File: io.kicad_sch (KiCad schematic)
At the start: 15 parts, among them J14 D IN1, J15 D IN2, J16 D IN3

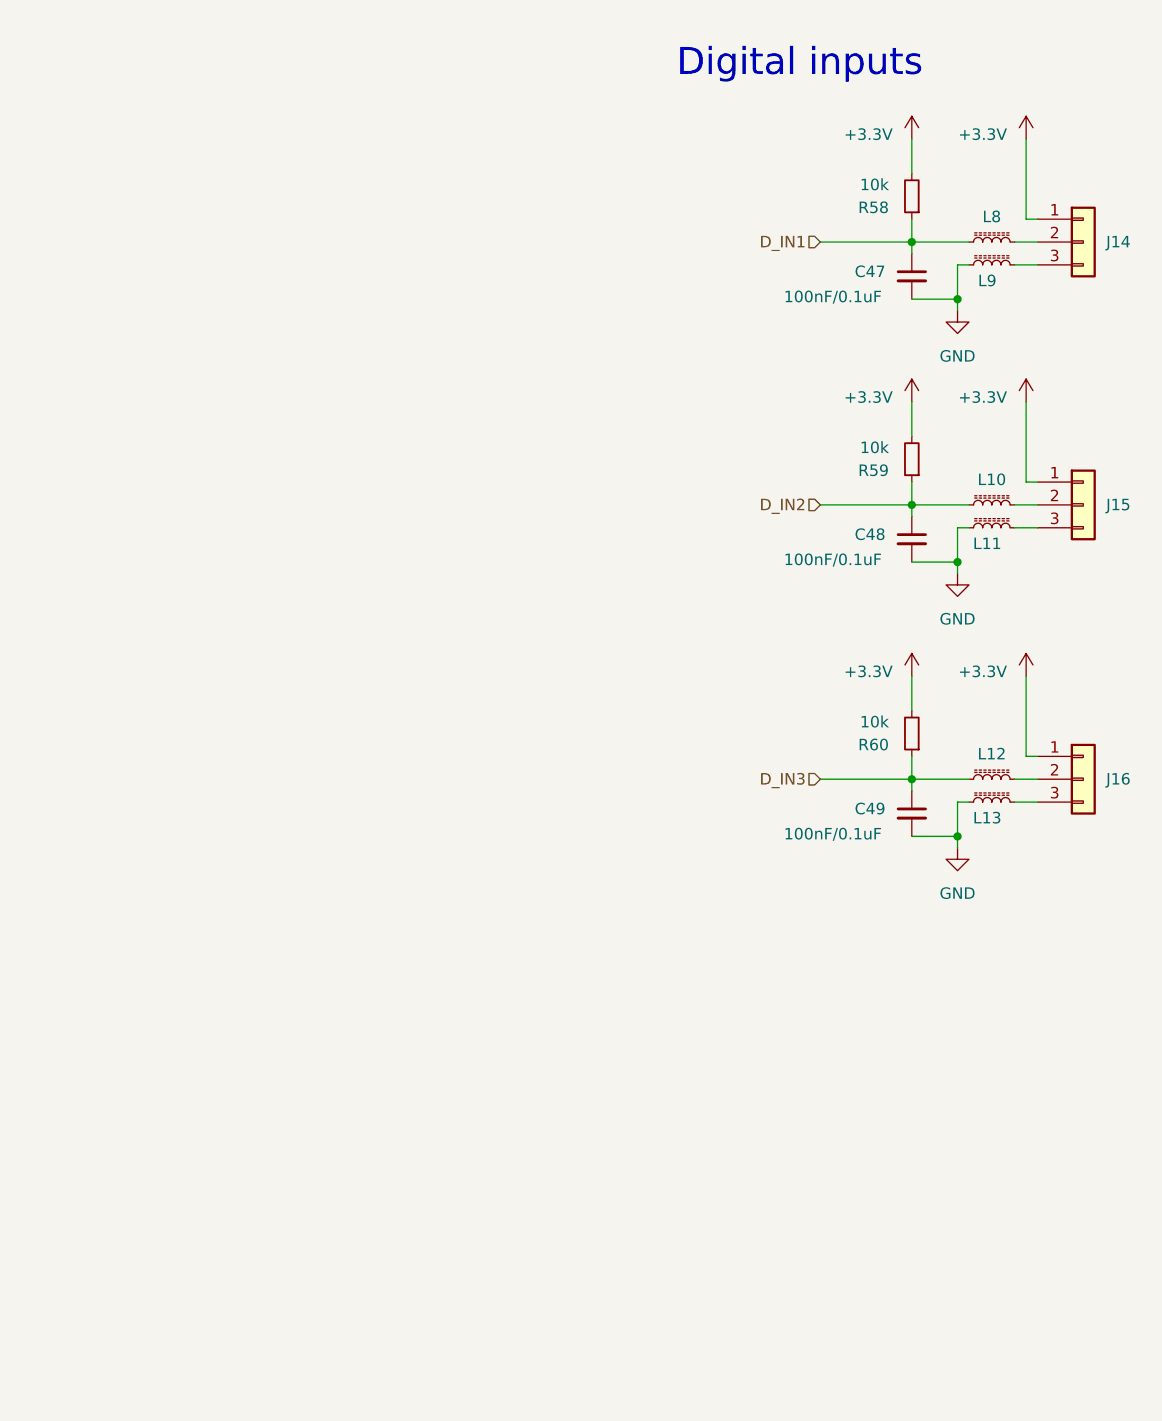
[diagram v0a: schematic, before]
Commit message: Add 1-Wire
Closes #29
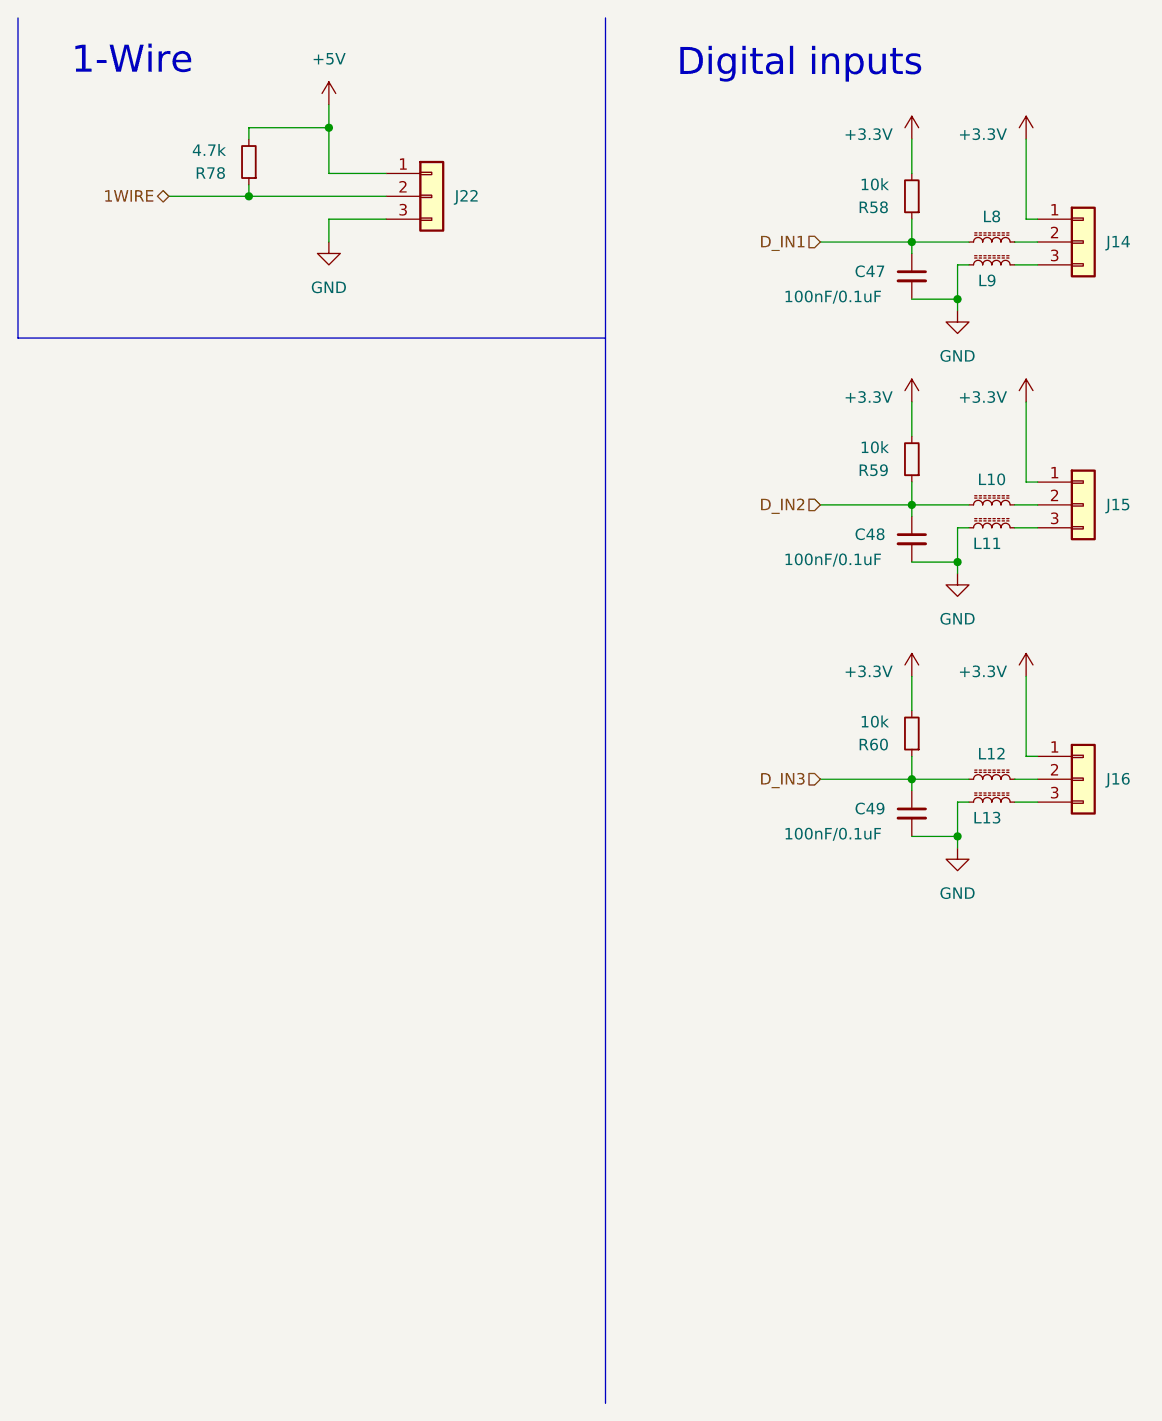
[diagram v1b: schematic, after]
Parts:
- added J22: 1-Wire, Connector_PinHeader_2.54mm:PinHeader_1x03_P2.54mm_Vertical, symbol Connector_Generic:Conn_01x03
- added R78: 4.7k, Resistor_SMD:R_0603_1608Metric, symbol Device:R_Small
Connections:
- net GND: now also J22.3 (Pin_3)
- new net +5V: J22.1 (Pin_1), R78.2
- new net 1WIRE: J22.2 (Pin_2), R78.1
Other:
- note added: "1-Wire"

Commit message: Update manufacturing positions and rotations of parts
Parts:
- J14, J15, J16: JLCPCB Position Offset (none) -> 0,2; JLCPCB Rotation Offset (none) -> 180
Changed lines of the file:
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@@
+			)
+		)
+		(property "JLCPCB Rotation Offset" "180"
+			(at 261.62 66.04 0)
+			(effects
+				(font
+					(size 1.27 1.27)
+				)
+				(hide yes)
+			)
+		)
+		(property "JLCPCB Position Offset" "0,2"
+			(at 261.62 66.04 0)
+			(effects
+				(font
+					(size 1.27 1.27)
+				)
+				(hide yes)
 			)
 		)
@@
 			)
 		)
+		(property "JLCPCB Rotation Offset" "180"
+			(at 261.62 36.83 0)
+			(effects
+				(font
+					(size 1.27 1.27)
+				)
+				(hide yes)
+			)
+		)
+		(property "JLCPCB Position Offset" "0,2"
+			(at 261.62 36.83 0)
+			(effects
+				(font
+					(size 1.27 1.27)
+				)
+				(hide yes)
+			)
+		)
 		(pin "2"
 		)
@@
 			(at 261.62 96.52 0)
 			(effects
+				(font
+					(size 1.27 1.27)
+				)
+				(hide yes)
+			)
+		)
+		(property "JLCPCB Rotation Offset" "180"
+			(at 261.62 96.52 0)
+			(effects
+				(font
+					(size 1.27 1.27)
+				)
+				(hide yes)
+			)
+		)
+		(property "JLCPCB Position Offset" "0,2"
+			(at 261.62 96.52 0)
+			(effects

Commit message: Include THT components in manufacturing
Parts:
- J14, J15, J16: now in the parts list
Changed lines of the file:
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@@
 		(unit 1)
 		(exclude_from_sim no)
-		(in_bom no)
+		(in_bom yes)
 		(on_board yes)
 		(dnp no)
@@
 		(unit 1)
 		(exclude_from_sim no)
-		(in_bom no)
+		(in_bom yes)
 		(on_board yes)
 		(dnp no)
@@
 		(unit 1)
 		(exclude_from_sim no)
-		(in_bom no)
-		(on_board yes)
-		(dnp no)
+		(in_bom yes)
+		(on_board yes)
+		(dnp no)
